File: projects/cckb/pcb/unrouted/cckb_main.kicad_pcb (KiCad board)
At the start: 2 copper layers, 285.8 x 95.3 mm, 124 parts, among them SW1 PG1350, SW10 PG1350, SW11 PG1350, SW12 PG1350, SW13 PG1350, SW14 PG1350, SW15 PG1350, SW16 PG1350, SW17 PG1350, SW18 PG1350, SW19 PG1350, SW2 PG1350, SW20 PG1350, SW21 PG1350, SW22 PG1350, SW23 PG1350, SW24 PG1350, SW25 PG1350, SW26 PG1350, SW27 PG1350, SW28 PG1350, SW29 PG1350, SW3 PG1350, SW30 PG1350, SW31 PG1350, SW32 PG1350, SW33 PG1350, SW34 PG1350, SW35 PG1350, SW36 PG1350, SW37 PG1350, SW38 PG1350, SW39 PG1350, SW4 PG1350, SW40 PG1350, SW41 PG1350, SW42 PG1350, SW43 PG1350, SW44 PG1350, SW45 PG1350, SW46 PG1350, SW47 PG1350, SW48 PG1350, SW49 PG1350, SW5 PG1350, SW50 PG1350, SW51 PG1350, SW52 PG1350, SW53 PG1350, SW54 PG1350, SW55 PG1350, SW56 PG1350, SW57 PG1350, SW58 PG1350, SW59 PG1350, SW6 PG1350, SW60 PG1350, SW61 PG1350, SW62 PG1350, SW7 PG1350, SW8 PG1350, SW9 PG1350

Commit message: CCKB: 基板・プレート・ケースの境界を凍結する（角・取付・電源スイッチ・スタビの逃げ・分割・高さ）
- spec.py: 外形（壁 1.6・隙 0.5 → 289.95×99.45）・高さ（床 1.6・下の空き 1.8・基板 1.6・縁 +7.0）・
  XIAO（公式 STEP の実寸・表に平ら・USB の口は外面から 0.3）・電池ホルダ BS-16-B4AK003・
  電源スイッチ MK-12C02-G025（裏・右端）・スタビの逃げ（輪郭＋0.5）・取付 10（下から M2×6 皿＋
  基板上のナット）・支え 38・プレートの分割（キーの境目）・トレイの継ぎ目（案 C）
- interface.py: 上の値から形を作る（図・探索・検査・基板の次の段が共有。寸法は持たない）
- tools/: 生成した基板の世界座標の書き出し（KiCad の Python）・取付の探索・図
- tests/test_cckb_interface.py: XIAO ↔ 公式 STEP、取付と支え ↔ いま生成した基板、プレートの
  分割 ↔ 生成した立体、を突き合わせる。各検査に故意に壊して落ちる検査。O7（スタビのキーの
  ダイオードが逃げ穴にかかる）は strict xfail で見張る
- 未配線の基板を作り直した（取付穴 10。DRC 違反 0・警告 silk_edge_clearance 2）

Co-Authored-By: Claude Opus 5.5 (1M context) <noreply@anthropic.com>
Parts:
- added H0: MountingHole_2.2mm_M2, MountingHole_2.2mm_M2, F.Cu at (10.8, 80.4)
- added H1: MountingHole_2.2mm_M2, MountingHole_2.2mm_M2, F.Cu at (33.8, 79.9)
- added H2: MountingHole_2.2mm_M2, MountingHole_2.2mm_M2, F.Cu at (11.8, 100.4)
- added H3: MountingHole_2.2mm_M2, MountingHole_2.2mm_M2, F.Cu at (31.4, 131.8)
- added H4: MountingHole_2.2mm_M2, MountingHole_2.2mm_M2, F.Cu at (82.3, 140.9)
- added H5: MountingHole_2.2mm_M2, MountingHole_2.2mm_M2, F.Cu at (127.3, 140.9)
- added H6: MountingHole_2.2mm_M2, MountingHole_2.2mm_M2, F.Cu at (198.3, 140.9)
- added H7: MountingHole_2.2mm_M2, MountingHole_2.2mm_M2, F.Cu at (243.8, 121.4)
- added H8: MountingHole_2.2mm_M2, MountingHole_2.2mm_M2, F.Cu at (266.8, 79.9)
- added H9: MountingHole_2.2mm_M2, MountingHole_2.2mm_M2, F.Cu at (287.8, 106.9)
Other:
- board size 285.8 x 95.3 mm -> 286.4 x 95.9 mm

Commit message: CCKB: 回路をデータに（circuit.py）・部品のフットプリントと配置（pcb_extra.py）・行列の配線の計画・O7 の解決
- circuit.py: 全部品と全ネットを名前で宣言。pinmap を通してパッドを引く（XIAO の BAT には何も繋がない）
- lib: XIAO の表面実装（公式 STEP を測った）・MK-12C02-G025（LCSC のフットプリントを図面と照合）・
  BS-16-B4AK003（図面 MY-CP-0085）・ふたの柱の穴
- pcb_extra.py: スタビの逃げ穴 8・XIAO/ホルダ（表）・電源スイッチと電子部品（裏）・アンテナの禁止域・
  XIAO の下の表の銅の禁止・縁と逃げ穴の配線禁止の帯・ネットクラス POWER
- matrix_routes.py: 行（裏）・列（表）・スイッチ→ダイオード・XIAO から行のバスまでを板のパッドから決まった形で。
  板の物との間隔と自分どうしの衝突を自分で確かめる。取付の 5 条件の「通り道」もこれを使う
  （段階 1 の直線の通り道はボスと中心穴を貫いていた）
- O7: スタビのキー 4 つのダイオードを中心穴の下へ横置き（逃げ穴から 0.405）。strict xfail を
  0.3 以上の検査に置き換え、前の位置に戻すと落ちる検査を足した
- spec: 電源スイッチのランドを取り込んだフットプリントの値に（PSW_TERM_EXT 1.58・PSW_LAND_L 8.3）

Co-Authored-By: Claude Opus 5.5 (1M context) <noreply@anthropic.com>
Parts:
- added BT1: BS-16-B4AK003, BAT_BS-16-B4AK003, F.Cu at (278.5, 138.6)
- added C_U1: 0.1uF, C_0805_2012Metric, B.Cu at (67.8, 105.9)
- added C_U2: 0.1uF, C_0805_2012Metric, B.Cu at (220.2, 105.9)
- added D_PWR: B5819W, D_SOD-123, B.Cu at (27.0, 125.8)
- added H_LID: Hole_6.0, Hole_NPTH_6.0mm, F.Cu at (251.0, 138.6)
- added R_HI: 1M, R_0805_2012Metric, B.Cu at (9.10, 127.7)
- added R_LO: 1M, R_0805_2012Metric, B.Cu at (9.10, 124.9)
- added SW_PWR: MK-12C02-G025, SW_MK-12C02-G025, B.Cu at (291.3, 143.4)
- added U1: SN74LVC595APWR, TSSOP-16_4.4x5mm_P0.65mm, B.Cu at (73.8, 108.2)
- added U2: SN74LVC595APWR, TSSOP-16_4.4x5mm_P0.65mm, B.Cu at (226.2, 108.2)
- added U_MCU: XIAO_nRF52840, XIAO_nRF52840_SMD, F.Cu at (17.4, 138.1)
- moved D42 4.41 mm to (277.0, 102.9), turned to 0 degrees
- moved D58 4.41 mm to (110.3, 141.0), turned to 0 degrees
- moved D43 4.41 mm to (34.1, 121.9), turned to 0 degrees
- moved D60 4.41 mm to (181.7, 141.0), turned to 0 degrees
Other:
- outline, holes or cut-outs redrawn

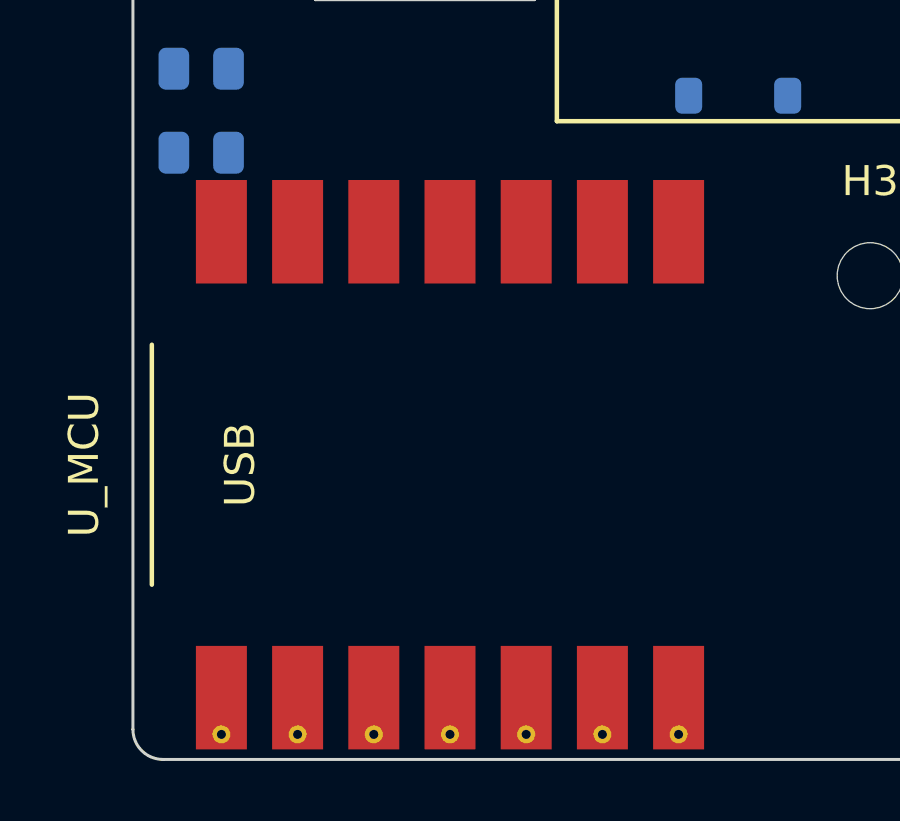
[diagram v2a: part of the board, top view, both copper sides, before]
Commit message: CCKB 監査の直し（R1〜R6）: パッドの中のビアを根本から無くし、XIAO の裏の露出パッド 8 個と H3 のインサートの下の表の銅を 0 に、電源スイッチを手はんだに、トレイの隙を片側 0.5 に
- R1: route_pcb.Space.free() が同じネットのパッドを当てていなかった（C_U1・BT1 の GND パッドの中に縫いのビア）。全パッドの「ビアが掛からない」検査（XIAO の D0〜D6 だけ名指しで例外）
- R2: SW_PWR を NOT_ASSEMBLED に（BOM 5 行・CPL 69 行）。Fabrication Toolkit の CPL を EasyEDA の原点とパッドで置き直して板と比べる検査
- R3: 露出パッド 8 個を STEP と Seeed 公式フットプリントで確定（spec.XIAO_BOTTOM_PADS）。XIAO のパッドを縁から内 2.2 に、禁止域を 8 個＋0.3 に
- R6: H3 のまわりに表の禁止域（半径 1.9）
- R5: spec.CASE_PCB_GAP 0.5 を interface が 1 か所で読む。外面は動かさず壁 1.3・窪み 0.9
- R7: パッド内ビア φ0.7・0805 と手はんだの GND をサーマル・ビア 1 本の長い GND の島に 2 本目
- 指紋がパッドの形とルール領域を見ない穴を、項目の比較と unrouted_sha256 で塞いだ

Co-Authored-By: Claude Opus 5.5 (1M context) <noreply@anthropic.com>
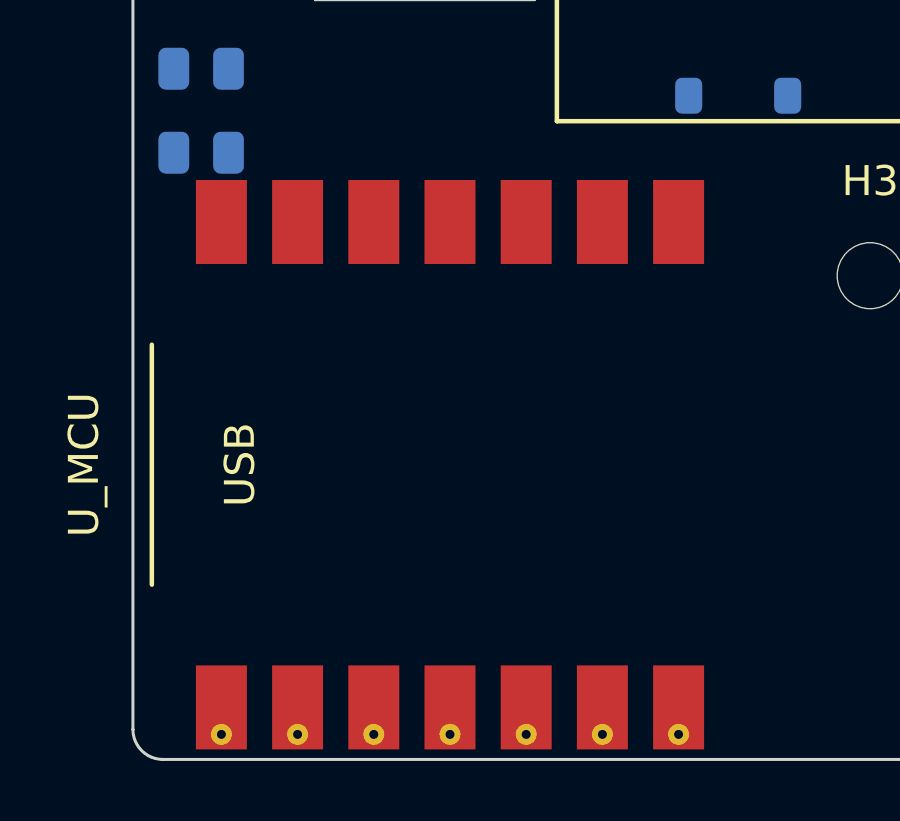
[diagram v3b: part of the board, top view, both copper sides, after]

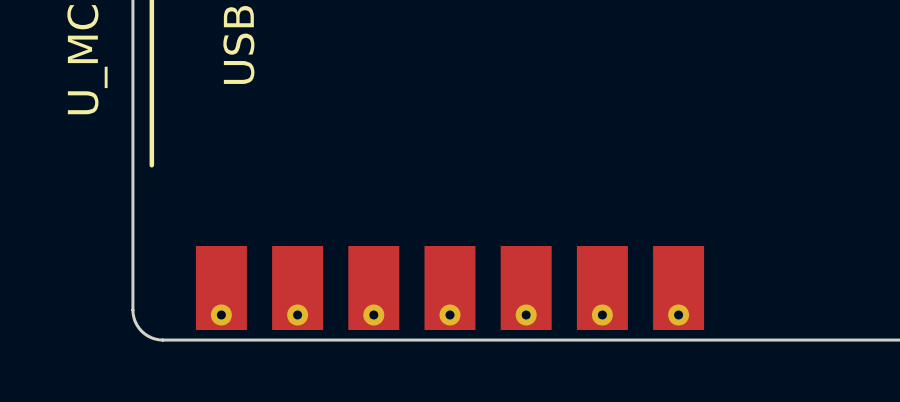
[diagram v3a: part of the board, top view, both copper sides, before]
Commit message: CCKB 2 回目の監査の直し（S1〜S3）: 金属が当たる 10 か所に禁止域、CS の 1 本だけ置き直し、D_PWR の既定を BAT46W に
- S1: interface.metal_on_pcb が取付の穴 11 ごとに金属の当たる面を高さで判定（上面にナット 9・H3 のインサート、下面 0）。
  METAL_KEEPOUT を 10 か所に。route_pcb.py --reroute CS で前の板の配線を持ってきて、H5・H6 のナットの下の CS の 1 本だけを
  決まった形で置き直した（ほかの 89 網は線・ビアとも前の板と同じ）。検査は板から穴を数え、塗った後の銅まで見る
- S2: 逆流を「逆漏れ − 分圧が吸う電流」・Vf を保証値どうしで比べ直し、既定を BAT46W C54110 に（利用者が発注前に決める・O12）
- S3: 手はんだの部品のパッドからペーストを外した（B_Paste 173 → 166）・パッド内ビア φ0.8・DRC の警告の数を固定・
  USB のシールドの長穴 4 個を数えに・つまみ 1.55×1.1・手順書と台帳

Co-Authored-By: Claude Opus 5.5 (1M context) <noreply@anthropic.com>
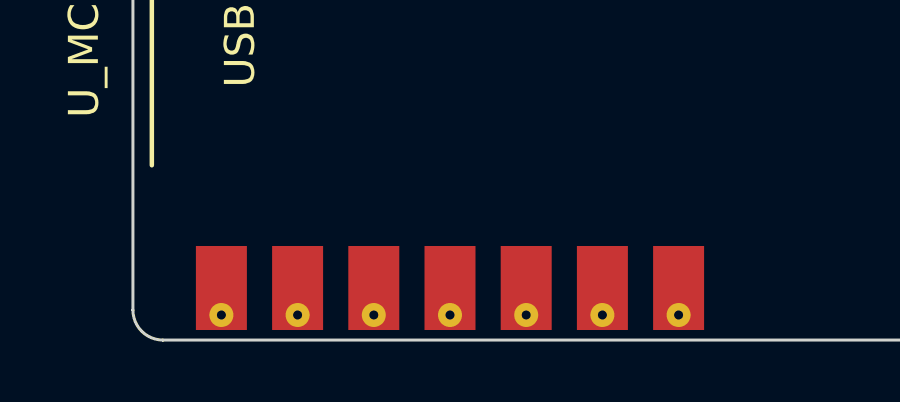
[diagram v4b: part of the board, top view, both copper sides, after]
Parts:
- D_PWR: value B5819W -> BAT46W

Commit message: CCKB 電源スイッチを秋月 SS-12D00G3（表・レバーが上）へ: 基板・ケース・組み立て・検査
- 利用者の決定（2026-09-24）で MK-12C02-G025（LCSC・裏・横のつまみ）から置き換え
- 基板: SW_PWR を表・スルーホールで (141.225, -38.6)、BT1 を左へ 3.8（124.7）。
  網 VBAT_IN・VBAT_SW の右の角だけ引き直し（ほかの 88 網は前の板と同じ）。
  枠の爪の下に表の銅の禁止域 PSW_TAB_KEEPOUT。位置決めの穴が無くなり DRC_SEVERITY を消した
  （DRC 違反 0・未配線 0・警告 3）。前のフットプリントと EasyEDA の C778186 を消した
- route_pcb: --clear（動かした部品の周りの前の線を捨てる）・行き止まりの削除・
  SES の取り込みで動いた部品を元に戻す（A10 の 50nm の原因）・引き直す網を二重に戻さない
- ケース: 右の壁の切り欠き・窪み・ふたのひれを消し、右のふたにレバーの穴 6.4x2.4 と「ON ↑」の刻印
- 組み立て: スイッチを 1 つの立体に（足は 1.0 に切る）。爪の検査を上からに書き直し
- 爪の出 PSW_TAB 0.4 [暫定]（図面に寸法無し）でレバーの先は名目でふたの上面の 0.1 下・最悪 +0.2（O13）

Co-Authored-By: Claude Opus 5.5 (1M context) <noreply@anthropic.com>
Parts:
- removed the SW_PWR at (291.3, 143.4)
- added SW_PWR: SS-12D00G3, SW_SS-12D00G3, F.Cu at (291.2, 138.6)
- moved BT1 3.80 mm to (274.7, 138.6)

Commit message: CCKB を Choc V2 に: 基板を作り直して配線（DRC 違反 0・未配線 0）・高さ・床の止まり穴の出力
- spec: SWITCH=choc_v2・高さ 5.3/8.6・足の公差 0.2・中心の突起 3.30・床の止まり穴 0.4（UNDER_PCB 1.8 のまま）
- 行のバスを 3.35 下に（中心穴と位置決めの長穴の間）。スタビ・取付の穴の所だけ下へ回り道（matrix_routes.buses）
- 列が段の境目を渡る高さをずらせるように・XIAO から行 0〜2 は XIAO の下で左へ寄せてから上がる
- VBAT_SW の長い 1 本を決まった形で（POWER_RUNS）・D_PWR を XIAO の奥の縁の上へ
- 595 の OE を本体の下で GND の 8 番へ（ビア 1 本の OE が線に囲まれて浮いた）
- 長円の非めっき穴の縁に配線禁止の帯（NPTH_KEEPOUT）・縫いのビアは穴の実物の形で当てる
- 取付 H9 を Del の右下へ・H0 を 0.25 左へ・支え 8 本を動かした（当たり: 長穴・スタビの穴）
- interface.floor_pockets（突起 62・スタビの箱 8）をケースの段の出どころに
- 検査を V2 の値に。足の先と床の間が最悪 0.04 で高さ・剛性の検査 2 つは赤のまま（利用者の判断待ち）

Co-Authored-By: Claude Opus 5.5 (1M context) <noreply@anthropic.com>
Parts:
- added ST42: Stab_Kailh_Choc_V2_Screw_2u, Stab_Kailh_Choc_V2_Screw_2u, F.Cu at (271.4, 100.0)
- added ST43: Stab_Kailh_Choc_V2_Screw_2u, Stab_Kailh_Choc_V2_Screw_2u, F.Cu at (28.6, 119.0)
- added ST58: Stab_Kailh_Choc_V2_Screw_2u, Stab_Kailh_Choc_V2_Screw_2u, F.Cu at (104.8, 138.1)
- added ST60: Stab_Kailh_Choc_V2_Screw_2u, Stab_Kailh_Choc_V2_Screw_2u, F.Cu at (176.2, 138.1)
- SW1, SW10, SW11, SW12, SW13, SW14, SW15, SW16, SW17, SW18, SW19, SW2, SW20, SW21, SW22, SW23, SW24, SW25, SW26, SW27, SW28, SW29, SW3, SW30, SW31, SW32, SW33, SW34, SW35, SW36, SW37, SW38, SW39, SW4, SW40, SW41, SW42, SW43, SW44, SW45, SW46, SW47, SW48, SW49, SW5, SW50, SW51, SW52, SW53, SW54, SW55, SW56, SW57, SW58, SW59, SW6, SW60, SW61, SW62, SW7, SW8, SW9: value PG1350 -> PG1353; footprint SW_Kailh_Choc_V1 -> SW_Kailh_Choc_V2_Slot
- moved H9 21.9 mm to (289.4, 85.0)
- moved D42 4.20 mm to (278.5, 99.0), turned to 90 degrees
- moved D58 4.20 mm to (111.9, 137.1), turned to 90 degrees
- moved D43 4.20 mm to (35.7, 118.0), turned to 90 degrees
- moved D60 4.20 mm to (183.3, 137.1), turned to 90 degrees
- moved D_PWR 2.83 mm to (26.0, 128.4)
- moved D1 0.50 mm to (23.7, 60.9)
- moved D10 0.50 mm to (195.2, 60.9)
- moved D11 0.50 mm to (214.2, 60.9)
- moved D12 0.50 mm to (233.3, 60.9)
- moved D13 0.50 mm to (252.3, 60.9)
- moved D14 0.50 mm to (271.4, 60.9)
- moved D15 0.50 mm to (290.4, 60.9)
- moved D16 0.50 mm to (28.5, 79.9)
- moved D17 0.50 mm to (52.3, 79.9)
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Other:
- outline, holes or cut-outs redrawn

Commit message: CCKB V2 の位置決めの穴を丸 φ2.1 に（JLC の長円の比）・名札・床の穴: 板 6b886491（DRC 違反 0・未配線 0・警告 0）
2026-09-26 の V2 監査 C 重要 1: 非めっきの長円 78 個が JLC の「長円の長さ ≧ 幅 × 2」を満たさない。
- 位置決めの長円 62（1.6 × 2.0・比 1.25）を丸 φ2.1 に。足跡を SW_Kailh_Choc_V2_Slot → SW_Kailh_Choc_V2_Common。
  3 枚の図の推奨の穴（標準 φ1.60・静音 長円 2.0 × 1.5）の和を JLC の丸穴の公差 −0.08 でも含む。底面図の「5.50」は
  穴の中の突起と読み直した（静音 茶の図を 600dpi で）。突起は公差の最悪でも入る
- スタビのねじ・爪の長円 16 は保留（スタビの品を選び直し中。Kailh 公式 CPG1353G24D01）。検査は数を固定した例外 16
- 検査: 板の穴の比（board_facts に drill_wh・slot）と、発注の道具が出した NPTH.drl の長円。前の板で落ちることを確かめた
- 配線は前の板（dae52e33）の信号線を route_pcb --reroute でそのまま持ってきた（全部を引き直すと COL5・COL6 が未配線）。
  route_pcb は計画が引く網（ROW*・SW*_D）を前の板から持ってこない・長円が無いとき NPTH_KEEPOUT を求めない
- C 軽微 3: D42・D43・D58・D60 の名札をダイオードの左へ（silk_edge_clearance 4 → 0）
- 床の止まり穴（位置決め）が丸 φ2.9 に → 支えの柱 4 本を 0.1・左奥の滑り止めを 0.2 動かした
- E 重要 4: 枠がスイッチを保持しないことを mech のコメントに

Co-Authored-By: Claude Opus 5.5 (1M context) <noreply@anthropic.com>
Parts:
- SW1, SW10, SW11, SW12, SW13, SW14, SW15, SW16, SW17, SW18, SW19, SW2, SW20, SW21, SW22, SW23, SW24, SW25, SW26, SW27, SW28, SW29, SW3, SW30, SW31, SW32, SW33, SW34, SW35, SW36, SW37, SW38, SW39, SW4, SW40, SW41, SW42, SW43, SW44, SW45, SW46, SW47, SW48, SW49, SW5, SW50, SW51, SW52, SW53, SW54, SW55, SW56, SW57, SW58, SW59, SW6, SW60, SW61, SW62, SW7, SW8, SW9: footprint SW_Kailh_Choc_V2_Slot -> SW_Kailh_Choc_V2_Common

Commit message: CCKB V2 スタビの穴を販売者の実測に（支点 ±11.9・丸 φ3.0 / φ4.0・半径 2.6 の禁止域）・プレート・キャップの受け口: 板 5f02d2b0（DRC 違反 0・未配線 0・警告 0）
- 基板: ねじ φ3.0 を y −6.2・爪 φ4.0 を y +8.24（丸い非めっき）・箱の穴 支点 ±3.0 × ±4.0。穴の中心から 2.6 は GND のベタ以外の銅なし（STAB_HOLE_KEEPOUT）
- 長円の例外 HELD_STAB_SLOTS を消した（板・ドリルのファイルとも長円 0）。発注する板を決めた数と比べる検査と壊す検査 7 通り
- 配線: 行のバスは禁止域の下を回る（キー中心の 8.95 下）。左 Shift の左のねじの禁止域で塞がった VBAT_SW・V3V3・SPI_MOSI と、行 2 の回り道に重なった COL14 を決まった形で（spec.FIXED_RUNS）
- プレート: 販売者の足跡の値に戻した（+0.1 を消した）。残した妥協 4 つ
- キャップ: 受け口を ±11.9・台 φ5.1 で 2.0 掴む（前 0.45）。coupon_stab_return。ねじの頭 φ3.7 × 1.5 と床の止まり穴 8・支え 2 本を動かした

Co-Authored-By: Claude Opus 5.5 (1M context) <noreply@anthropic.com>
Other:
- outline, holes or cut-outs redrawn
